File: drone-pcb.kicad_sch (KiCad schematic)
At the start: 24 parts, among them J1 Conn_01x03_Pin, J10 Conn_01x03_Pin, J2 Conn_01x02_Pin, J3 Conn_01x02_Pin, J4 Conn_01x02_Pin, J5 Conn_01x02_Pin, J6 Conn_01x02_Pin, J7 Conn_01x02_Pin, J8 USB_C_Receptacle_USB2.0_16P, J9 Conn_01x02_Pin, Q1 AO3400A, Q2 AO3400A, Q3 AO3400A, Q4 AO3400A, Q5 AO3400A, Q6 AO3400A, SW1 CK_KMS2xxGP, U1 RP2350A, U2 nRF24L01P

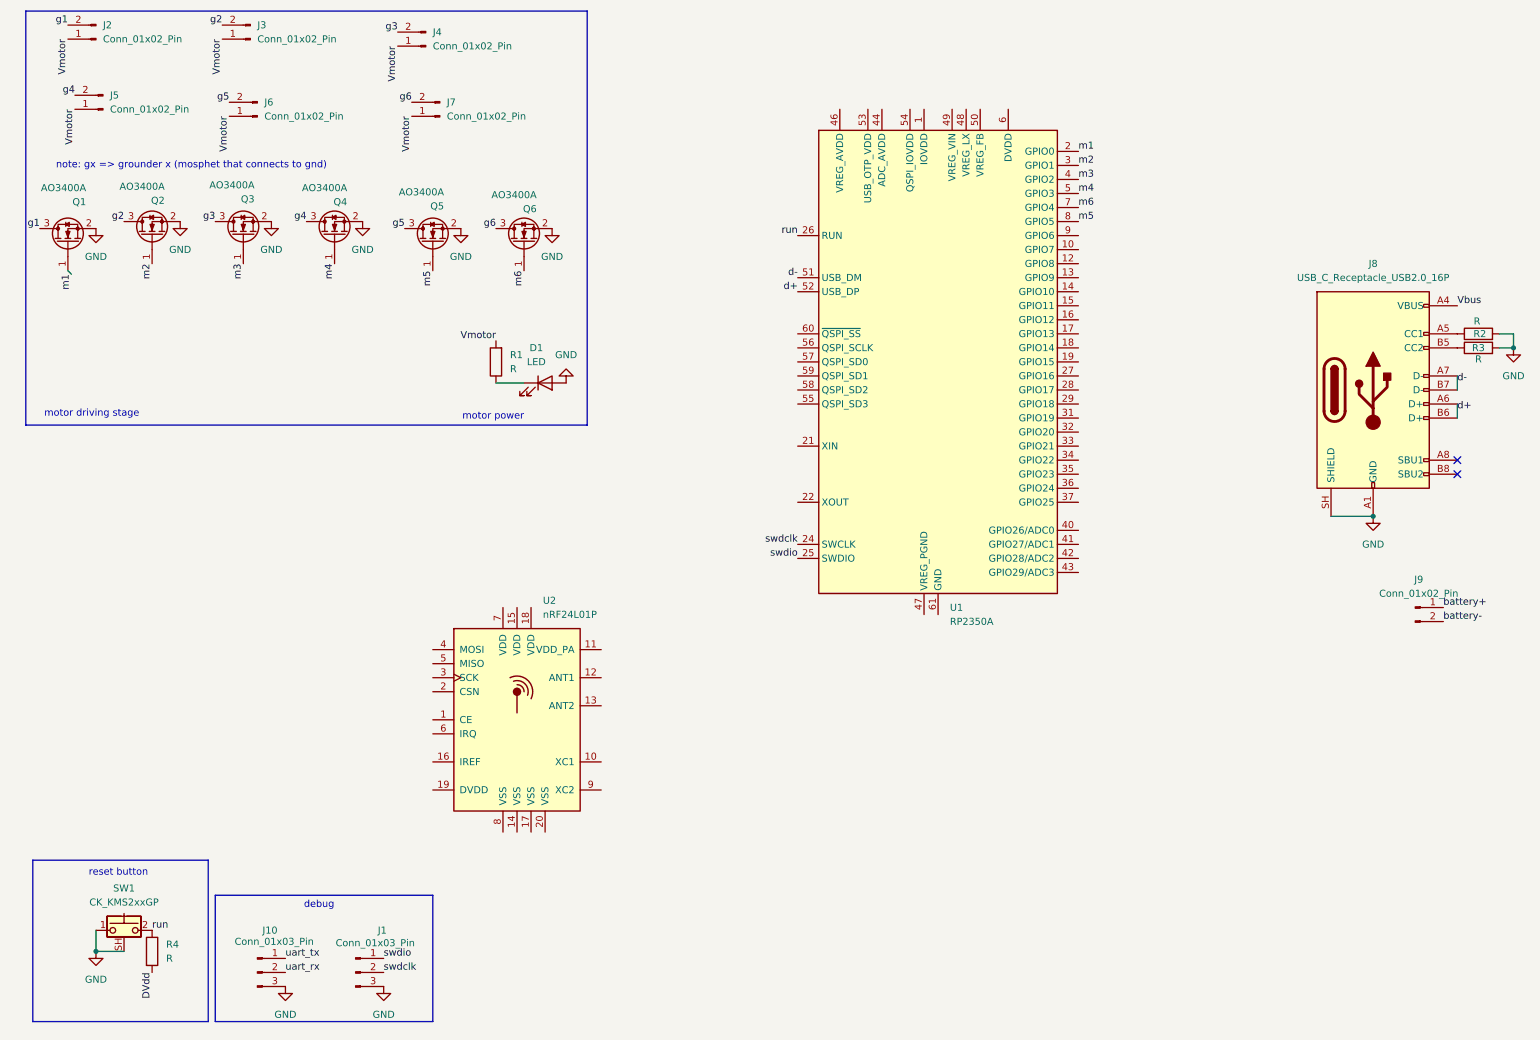
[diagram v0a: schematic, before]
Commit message: change to stm32f030c8tx, fix motor driving mosfet pulldown
reannotate the components, add resistance value to resistors, fix pulldown resistors on mosphet
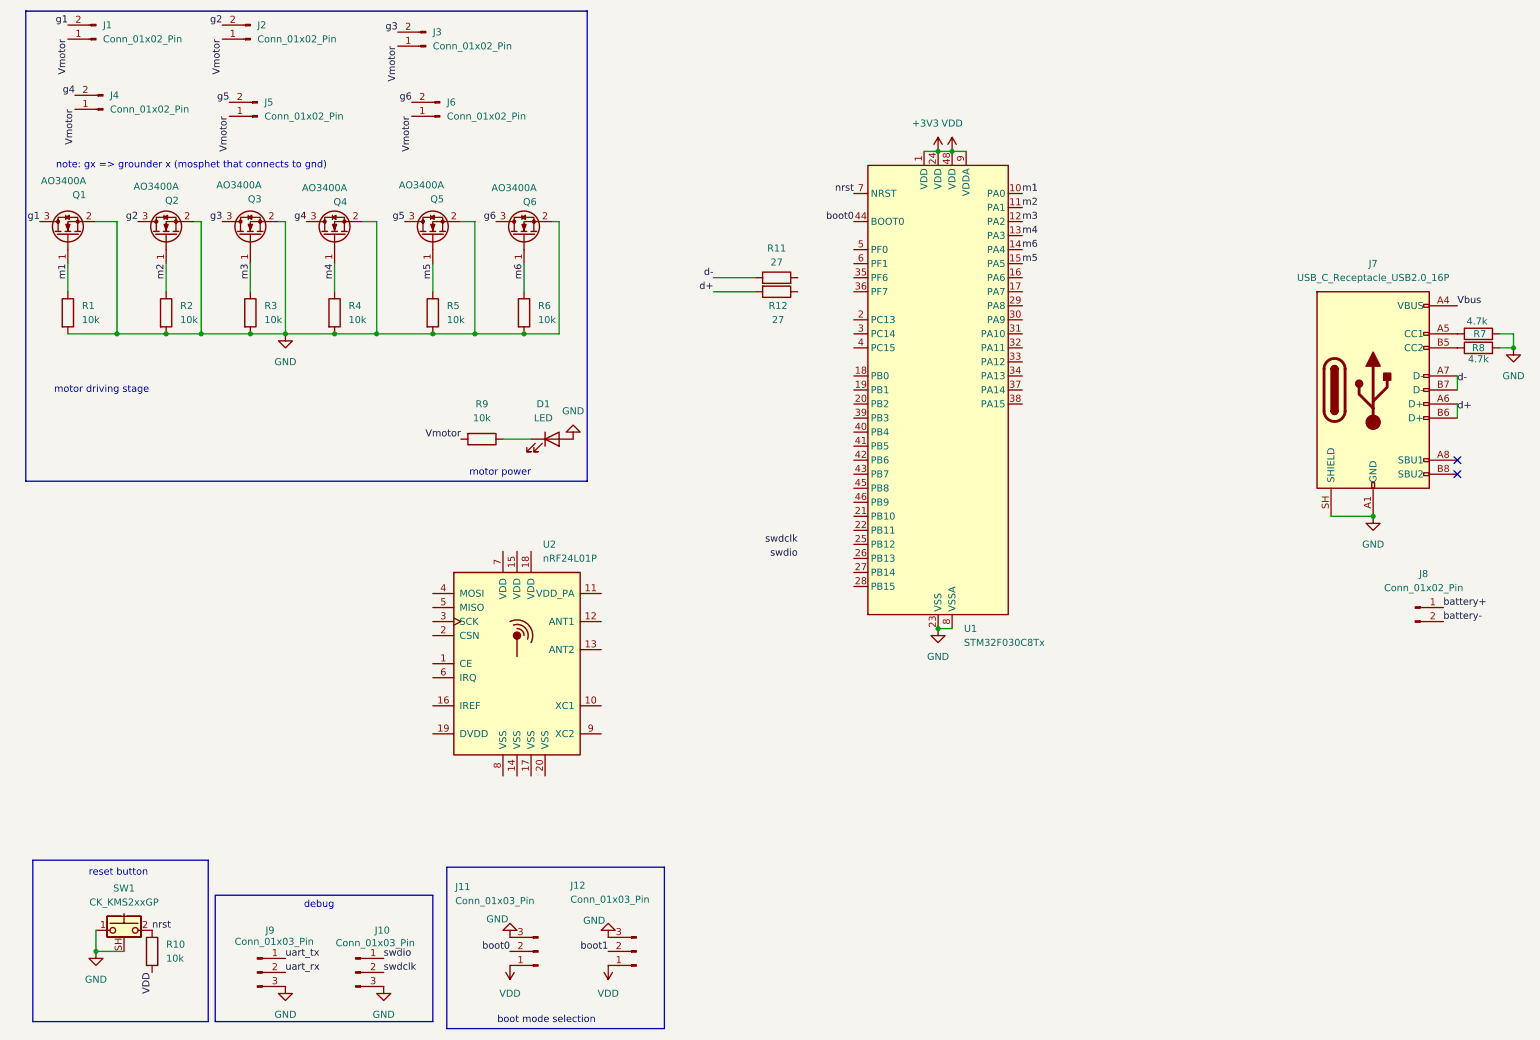
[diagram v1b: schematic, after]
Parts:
- removed U1: RP2350A, Package_DFN_QFN:QFN-60-1EP_7x7mm_P0.4mm_EP3.4x3.4mm, symbol MCU_RaspberryPi:RP2350A
- added J11, J12: Conn_01x03_Pin, Package_QFP:LQFP-48_7x7mm_P0.5mm, symbol Connector:Conn_01x03_Pin
- added R11, R12: 27, symbol Device:R
- added R2, R3, R4, R5, R6, R9: 10k, Package_DIP:DIP-8_W7.62mm, symbol Device:R
- added U1: STM32F030C8Tx, Package_QFP:LQFP-48_7x7mm_P0.5mm, symbol MCU_ST_STM32F0:STM32F030C8Tx
- R1: value R -> 10k
- R10: renamed from R4; value R -> 10k
- R7: renamed from R2; value R -> 4.7k
- R8: renamed from R3; value R -> 4.7k
- renumbered J2 to J1, J1 to J10, J3 to J2, J4 to J3, J5 to J4, J6 to J5, J7 to J6, J8 to J7, J9 to J8, J10 to J9
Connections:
- net GND: now also R1.2, J11.3 (Pin_3), J12.3 (Pin_3), R2.2, R3.2, R4.2, R5.2, R6.2, U1.23 (VSS), U1.47 (VSS), U1.8 (VSSA)
- net Vmotor: now also R9.2; no longer R1.2
- net d+: now also R12.2
- net d-: now also R11.1
- net m1: now also R1.1, U1.10 (PA0)
- net m2: now also R2.1, U1.11 (PA1)
- net m3: now also R3.1, U1.12 (PA2)
- net m4: now also R4.1, U1.13 (PA3)
- net m5: now also R5.1, U1.15 (PA5)
- net m6: now also R6.1, U1.14 (PA4)
- net at D1.1 (K): now also R9.1; no longer R1.1
- net DVdd renamed +3V3
- net +3V3: now also J11.1 (Pin_1), J12.1 (Pin_1), U1.1 (VDD), U1.24 (VDD), U1.48 (VDD), U1.9 (VDDA)
- net run renamed nrst
- net nrst: now also U1.7 (NRST)
- new net boot0: J11.2 (Pin_2), U1.44 (BOOT0)
- new net boot1: J12.2 (Pin_2)
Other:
- note added: "boot mode selection"
- moved on the sheet: Q1, Q2, Q3, Q5, Q6, U2

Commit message: LDO and BMS - not complete
added battery charging IC , not fully implemented, then added ldo regulator to convert battery voltage into power rail for the chips - not complete
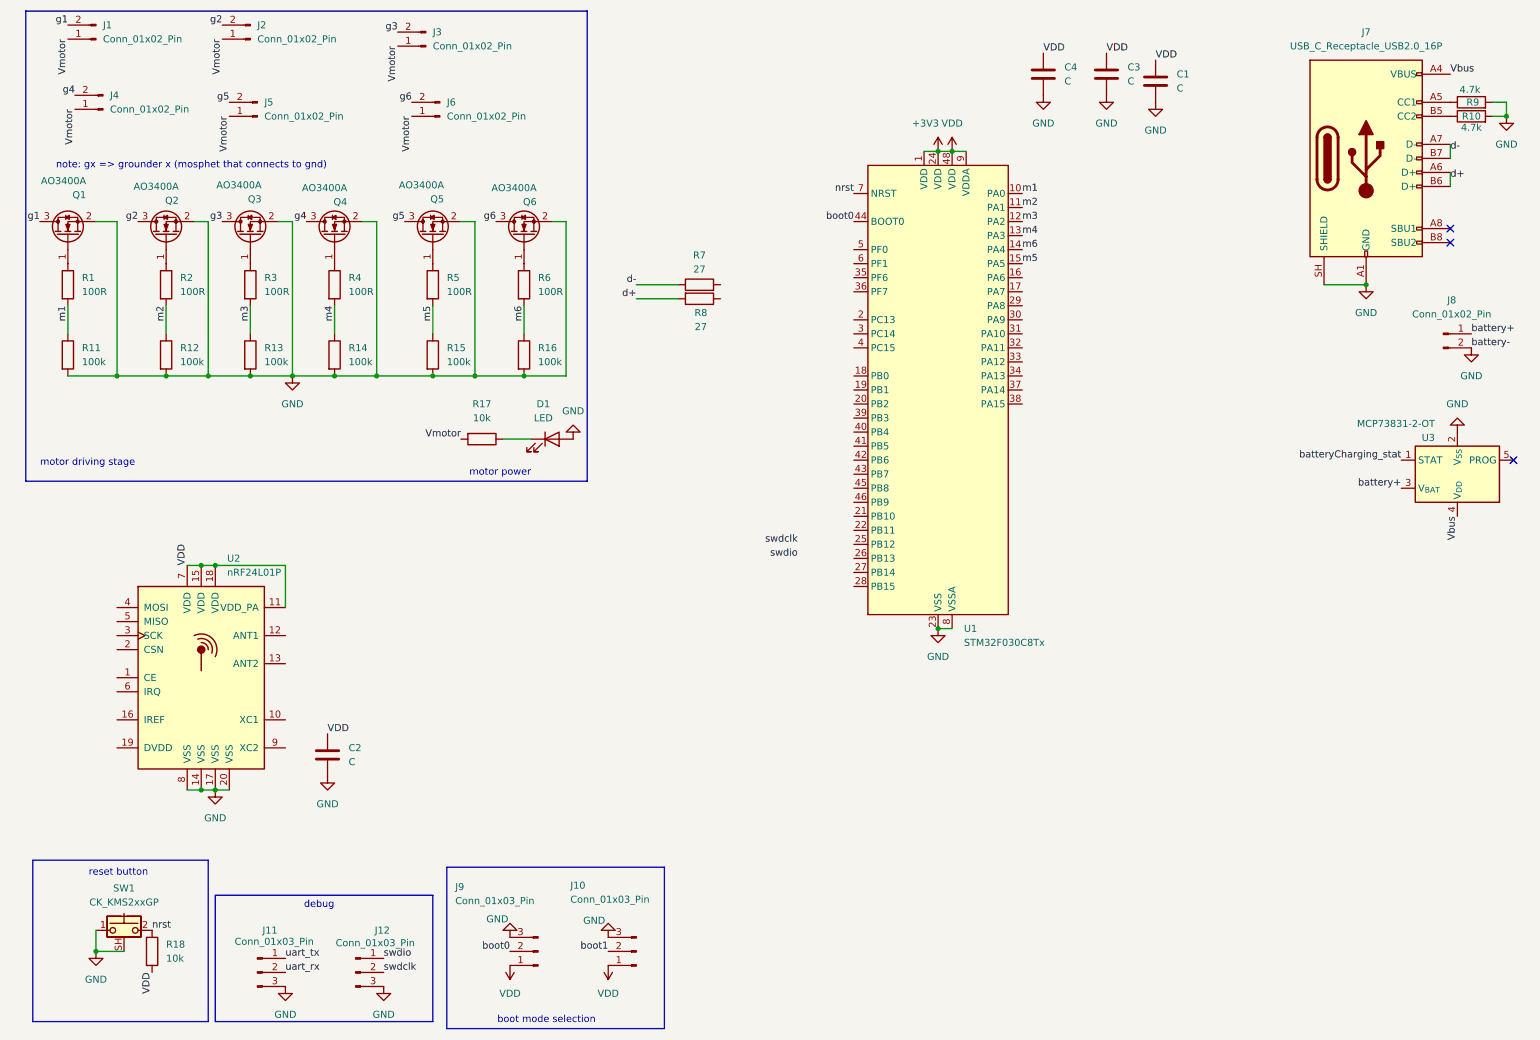
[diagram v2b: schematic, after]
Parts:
- added C1, C2, C3, C4: C, Package_SO:SOIC-8_3.9x4.9mm_P1.27mm, symbol Device:C
- added R1, R2, R3, R4, R5, R6: 100R, Package_DIP:DIP-8_W7.62mm, symbol Device:R
- added U3: MCP73831-2-OT, Package_TO_SOT_SMD:SOT-23-5, symbol Battery_Management:MCP73831-2-OT
- R11: renamed from R1; value 10k -> 100k
- R12: renamed from R2; value 10k -> 100k
- R13: renamed from R3; value 10k -> 100k
- R14: renamed from R4; value 10k -> 100k
- R15: renamed from R5; value 10k -> 100k
- R16: renamed from R6; value 10k -> 100k
- renumbered J12 to J10, J9 to J11, J10 to J12, J11 to J9, R8 to R10, R9 to R17, R10 to R18, R11 to R7, R12 to R8, R7 to R9
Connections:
- net battery- is gone; now on net GND: J8.2 (Pin_2)
- net +3V3: now also U2.11 (VDD_PA), U2.15 (VDD), U2.18 (VDD), U2.7 (VDD), C1.1, C2.1, C3.1, C4.1
- net GND: now also U2.14 (VSS), U2.17 (VSS), U2.20 (VSS), U2.8 (VSS), C1.2, C2.2, C3.2, C4.2, U3.2 (V_{SS})
- net Vbus: now also U3.4 (V_{DD})
- net battery+: now also U3.3 (V_{BAT})
- net m1: now also R1.2; no longer Q1.1 (G)
- net m2: now also R2.2; no longer Q2.1 (G)
- net m3: now also R3.2; no longer Q3.1 (G)
- net m4: now also R4.2; no longer Q4.1 (G)
- net m5: now also R5.2; no longer Q5.1 (G)
- net m6: now also R6.2; no longer Q6.1 (G)
- new net: Q1.1 (G), R1.1
- new net: Q3.1 (G), R3.1
- new net: Q2.1 (G), R2.1
- new net: Q4.1 (G), R4.1
- new net: Q5.1 (G), R5.1
- new net: Q6.1 (G), R6.1
- new net batteryCharging_stat: U3.1 (STAT)
- no-connect marks 2 -> 3
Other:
- moved on the sheet: J7, J8, R10, R11, R12, R13, R14, R15, R16, R7, R8, R9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

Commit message: assign footprints to resistors, add different ldo
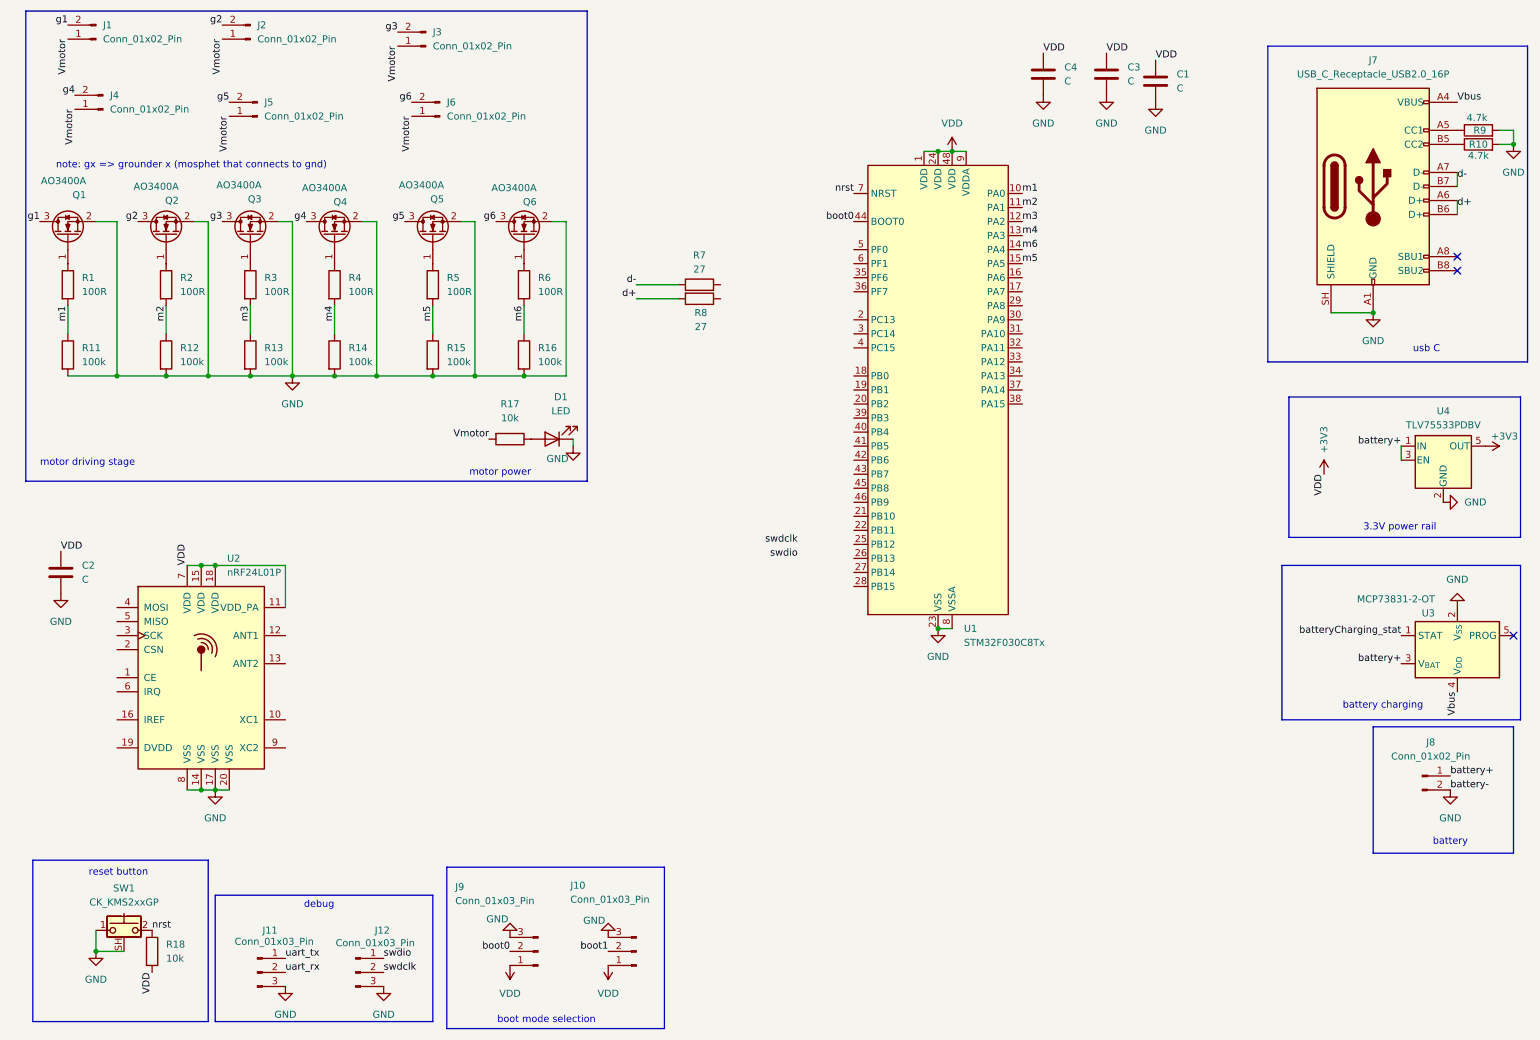
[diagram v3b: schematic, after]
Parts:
- added U4: TLV75533PDBV, Package_TO_SOT_SMD:SOT-23-5, symbol Regulator_Linear:TLV75533PDBV
- D1: footprint (none) -> LED_SMD:LED_0805_2012Metric_Pad1.15x1.40mm_HandSolder
- J1, J2, J3, J4, J5, J6: footprint (none) -> Connector_JST:JST_XH_S2B-XH-A-1_1x02_P2.50mm_Horizontal
- J7: footprint (none) -> Connector_USB:USB_C_Receptacle_HCTL_HC-TYPE-C-16P-01A
- R1, R11, R12, R13, R14, R15, R16, R17, R18, R2, R3, R4, R5, R6, R9: footprint Package_DIP:DIP-8_W7.62mm -> Resistor_SMD:R_0805_2012Metric_Pad1.20x1.40mm_HandSolder
- R10, R7, R8: footprint (none) -> Resistor_SMD:R_0805_2012Metric_Pad1.20x1.40mm_HandSolder
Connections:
- net +3V3: now also U4.5 (OUT)
- net GND: now also D1.1 (K), U4.2 (GND); no longer D1.2 (A)
- net battery+: now also U4.1 (IN), U4.3 (EN)
- net at R17.1: now also D1.2 (A); no longer D1.1 (K)
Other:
- note added: "3.3V power rail"
- note added: "battery"
- note added: "battery charging"
- note added: "usb C"
- moved on the sheet: C2, D1, J7, R10, R17, R9, U3

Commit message: add images, footprints
export schematics and pcb design into pdf files, add image of 3d rendering and put it in readme, correct the footprint of resistors, capacitors, headers, and battery connector
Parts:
- C1, C2, C3, C4: footprint Package_SO:SOIC-8_3.9x4.9mm_P1.27mm -> Capacitor_SMD:C_0805_2012Metric_Pad1.18x1.45mm_HandSolder
- J10, J9: footprint Package_QFP:LQFP-48_7x7mm_P0.5mm -> Connector_PinHeader_2.54mm:PinHeader_1x03_P2.54mm_Vertical
- J11, J12: footprint Package_TO_SOT_SMD:SOT-23 -> Connector_PinHeader_2.54mm:PinHeader_1x03_P2.54mm_Vertical
- J8: footprint Package_DFN_QFN:QFN-20-1EP_4x4mm_P0.5mm_EP2.5x2.5mm -> Connector_PinHeader_2.54mm:PinHeader_1x02_P2.54mm_Vertical
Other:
- company: (none) -> param foundation
- title: (none) -> drone-pcb
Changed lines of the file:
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@@
 	(generator_version "10.0")
 	(paper "A4")
+	(title_block
+		(title "drone-pcb")
+		(company "param foundation")
+		(comment 1 "designed in param makers adda")
+		(comment 2 "license: CERN-OHL-W V2.0")
+		(comment 3 "under development")
+	)
 	(rectangle
 		(start 13.97 166.37)
@@
 			)
 		)
-		(property "Footprint" "Package_SO:SOIC-8_3.9x4.9mm_P1.27mm"
+		(property "Footprint" "Capacitor_SMD:C_0805_2012Metric_Pad1.18x1.45mm_HandSolder"
 			(at 209.2452 27.94 0)
 			(hide yes)
@@
 			)
 		)
-		(property "Footprint" "Package_DFN_QFN:QFN-20-1EP_4x4mm_P0.5mm_EP2.5x2.5mm"
+		(property "Footprint" "Connector_PinHeader_2.54mm:PinHeader_1x02_P2.54mm_Vertical"
 			(at 265.43 151.13 0)
 			(hide yes)
@@
 			)
 		)
-		(property "Footprint" "Package_QFP:LQFP-48_7x7mm_P0.5mm"
+		(property "Footprint" "Connector_PinHeader_2.54mm:PinHeader_1x03_P2.54mm_Vertical"
 			(at 105.41 182.88 0)
 			(hide yes)
@@
 			)
 		)
-		(property "Footprint" "Package_SO:SOIC-8_3.9x4.9mm_P1.27mm"
+		(property "Footprint" "Capacitor_SMD:C_0805_2012Metric_Pad1.18x1.45mm_HandSolder"
 			(at 20.0152 118.11 0)
 			(hide yes)
@@
 			)
 		)
-		(property "Footprint" "Package_TO_SOT_SMD:SOT-23"
+		(property "Footprint" "Connector_PinHeader_2.54mm:PinHeader_1x03_P2.54mm_Vertical"
 			(at 54.61 186.69 0)
 			(hide yes)
@@
 			)
 		)
-		(property "Footprint" "Package_TO_SOT_SMD:SOT-23"
+		(property "Footprint" "Connector_PinHeader_2.54mm:PinHeader_1x03_P2.54mm_Vertical"
 			(at 72.39 186.69 0)
 			(hide yes)
@@
 			)
 		)
-		(property "Footprint" "Package_SO:SOIC-8_3.9x4.9mm_P1.27mm"
+		(property "Footprint" "Capacitor_SMD:C_0805_2012Metric_Pad1.18x1.45mm_HandSolder"
 			(at 197.8152 27.94 0)
 			(hide yes)
@@
 			)
 		)
-		(property "Footprint" "Package_SO:SOIC-8_3.9x4.9mm_P1.27mm"
+		(property "Footprint" "Capacitor_SMD:C_0805_2012Metric_Pad1.18x1.45mm_HandSolder"
 			(at 218.1352 29.21 0)
 			(hide yes)
@@
 			)
 		)
-		(property "Footprint" "Package_QFP:LQFP-48_7x7mm_P0.5mm"
+		(property "Footprint" "Connector_PinHeader_2.54mm:PinHeader_1x03_P2.54mm_Vertical"
 			(at 123.19 182.88 0)
 			(hide yes)

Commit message: svg images for board and schematic
inserted in README.md too
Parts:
- J8: footprint Connector_PinHeader_2.54mm:PinHeader_1x02_P2.54mm_Vertical -> Connector_JST:JST_XH_B2B-XH-A_1x02_P2.50mm_Vertical
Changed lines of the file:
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@@
 			)
 		)
-		(property "Footprint" "Connector_PinHeader_2.54mm:PinHeader_1x02_P2.54mm_Vertical"
+		(property "Footprint" "Connector_JST:JST_XH_B2B-XH-A_1x02_P2.50mm_Vertical"
 			(at 265.43 151.13 0)
 			(hide yes)
